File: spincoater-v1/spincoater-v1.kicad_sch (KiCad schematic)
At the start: 3 parts, among them J1 Conn_01x08_Pin, J2 SD_Card_Receptacle, U1 RASPBERRY_PI_PICO

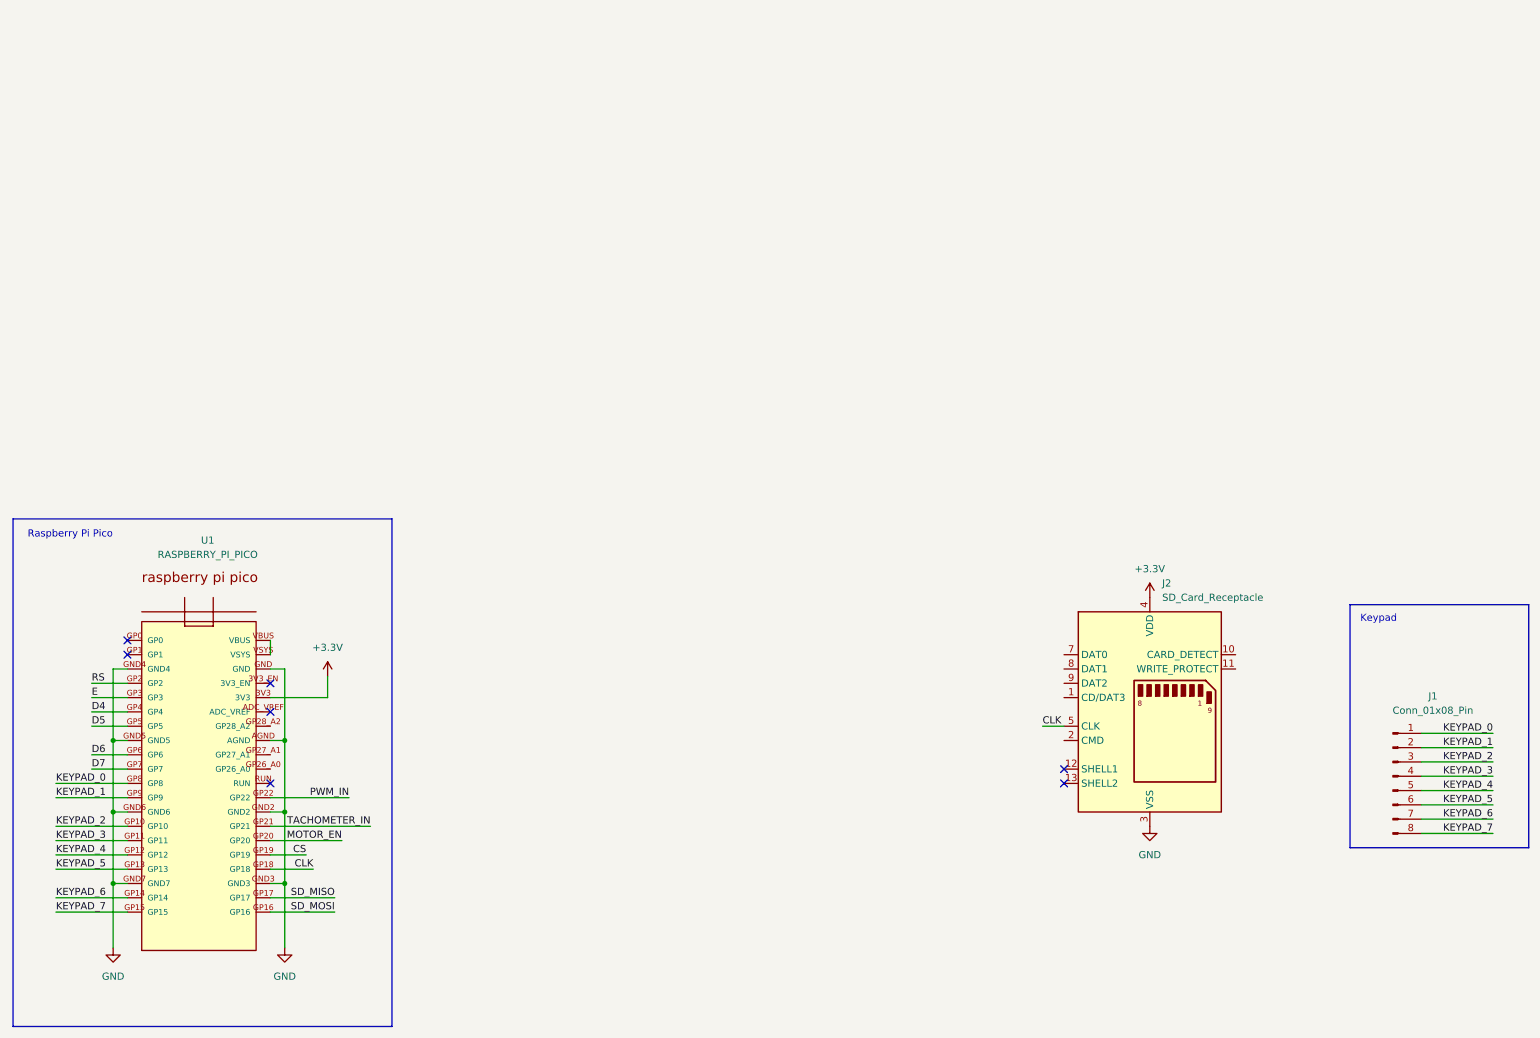
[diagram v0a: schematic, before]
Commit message: V1 schematic design of the spincoater completed.
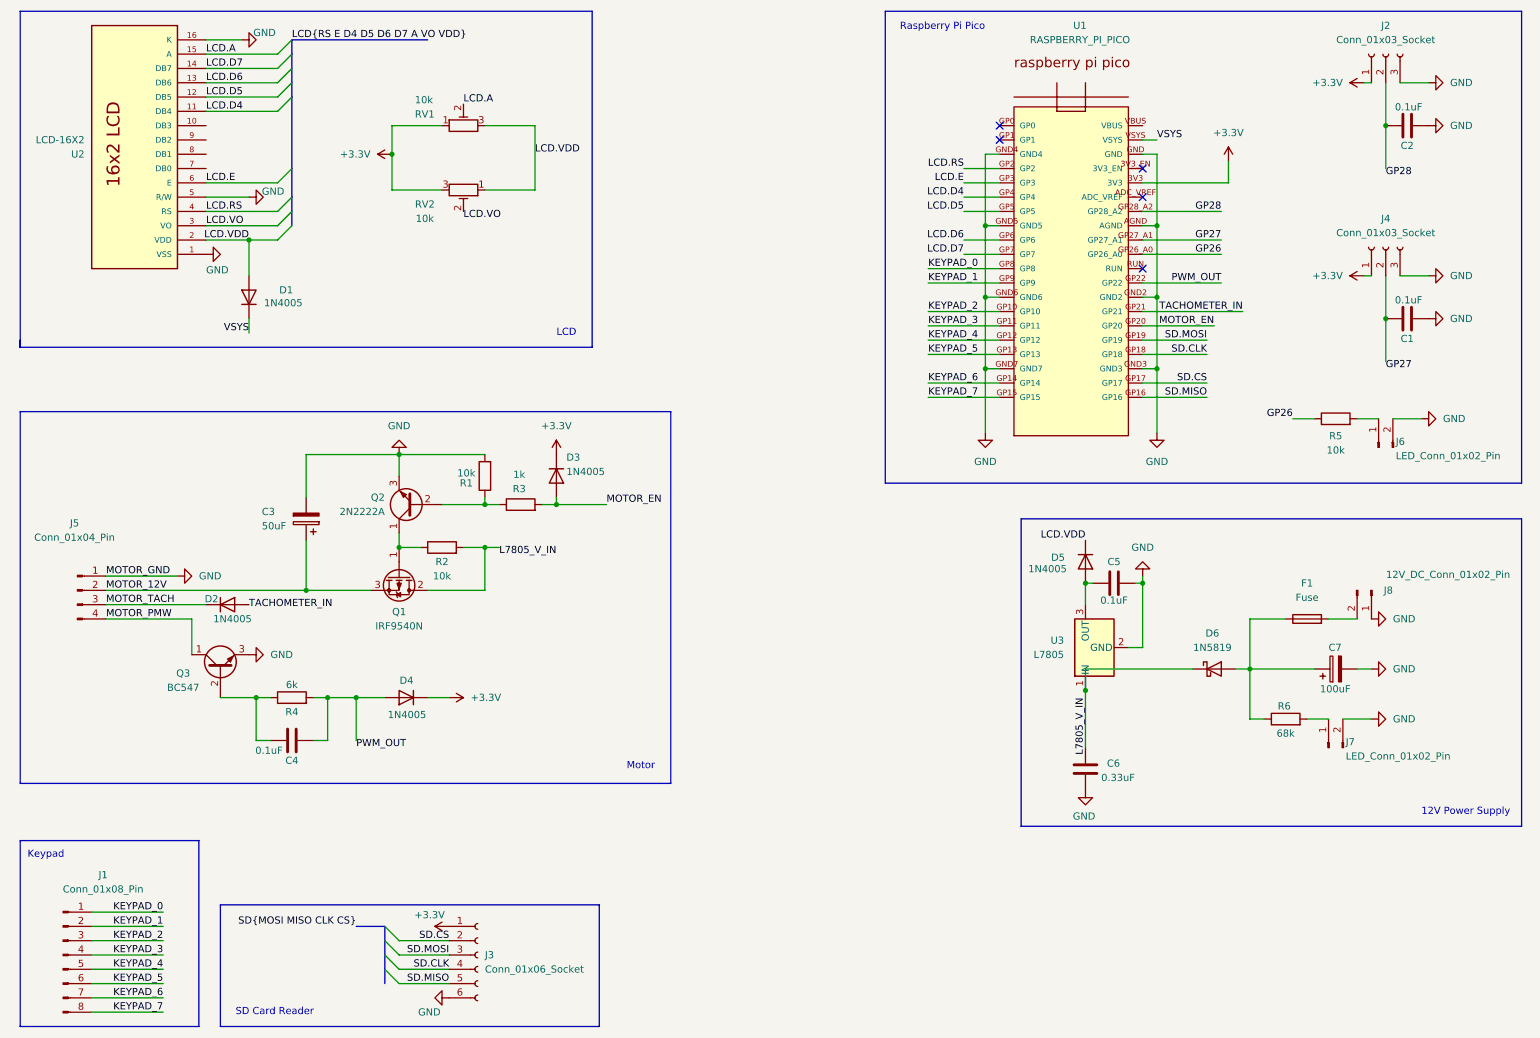
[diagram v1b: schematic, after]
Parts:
- removed J2: SD_Card_Receptacle, Connector_Card:SD_Card_Device_16mm_SlotDepth, symbol Connector:SD_Card_Receptacle
- added C1, C2, C4, C5: 0.1uF, symbol Device:C
- added C3: 50uF, symbol Device:C_Polarized
- added C6: 0.33uF, symbol Device:C
- added C7: 100uF, symbol Device:C_Polarized
- added D1, D2, D3, D4, D5: 1N4005, Diode_THT:D_DO-41_SOD81_P10.16mm_Horizontal, symbol Diode:1N4005
- added D6: 1N5819, Diode_THT:D_DO-41_SOD81_P10.16mm_Horizontal, symbol Diode:1N5819
- added F1: Fuse, symbol Device:Fuse
- added J2, J4: Conn_01x03_Socket, symbol Connector:Conn_01x03_Socket
- added J3: Conn_01x06_Socket, symbol Connector:Conn_01x06_Socket
- added J5: Conn_01x04_Pin, symbol Connector:Conn_01x04_Pin
- added J6, J7: LED_Conn_01x02_Pin, symbol Connector:Conn_01x02_Pin
- added J8: 12V_DC_Conn_01x02_Pin, symbol Connector:Conn_01x02_Pin
- added Q1: IRF9540N, Package_TO_SOT_THT:TO-220-3_Vertical, symbol Transistor_FET:IRF9540N
- added Q2: 2N2222A, Package_TO_SOT_THT:TO-92_Inline, symbol Transistor_BJT:BC547
- added Q3: BC547, Package_TO_SOT_THT:TO-92_Inline, symbol Transistor_BJT:BC547
- added R1, R2, R5: 10k, symbol Device:R
- added R3: 1k, symbol Device:R
- added R4: 6k, symbol Device:R
- added R6: 68k, symbol Device:R
- added RV1, RV2: 10k, symbol Device:R_Potentiometer_Trim
- added U2: LCD-16X2, LCD-16X2:MODULE_LCD-16X2, symbol LCD-16X2:LCD-16X2
- added U3: L7805, symbol Regulator_Linear:L7805
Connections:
- net +3.3V: now also D3.1 (K), D4.1 (K), J2.1 (Pin_1), J3.1 (Pin_1), J4.1 (Pin_1), RV1.1, RV2.3
- net GND: now also C1.2, C2.2, C3.2, C5.2, C6.1, C7.2, J2.3 (Pin_3), J3.6 (Pin_6), J4.3 (Pin_3), J5.1 (Pin_1), J6.2 (Pin_2), J7.2 (Pin_2), J8.1 (Pin_1), Q2.3 (E), Q3.3 (E), R1.2, U2.1 (VSS), U2.16 (K), U2.5 (R/W), U3.2 (GND)
- net MOTOR_EN: now also D3.2 (A), R3.2
- net TACHOMETER_IN: now also D2.2 (A)
- net GP26: now reaches U1.GP26_A0
- net GP26: now also R5.1
- net GP27: now reaches U1.GP27_A1
- net GP27: now also C1.1, J4.2 (Pin_2)
- net GP28: now reaches U1.GP28_A2
- net GP28: now also C2.1, J2.2 (Pin_2)
- net at U1.VBUS: no longer U1.VSYS
- net CLK renamed SD.CLK
- net SD.CLK: now also J3.4 (Pin_4)
- net CS renamed SD.MOSI
- net SD.MOSI: now also J3.3 (Pin_3)
- net D4 renamed LCD.D4
- net LCD.D4: now also U2.11 (DB4)
- net D5 renamed LCD.D5
- net LCD.D5: now also U2.12 (DB5)
- net D6 renamed LCD.D6
- net LCD.D6: now also U2.13 (DB6)
- net D7 renamed LCD.D7
- net LCD.D7: now also U2.14 (DB7)
- net E renamed LCD.E
- net LCD.E: now also U2.6 (E)
- net PWM_IN renamed PWM_OUT
- net PWM_OUT: now also C4.2, D4.2 (A), R4.2
- net RS renamed LCD.RS
- net LCD.RS: now also U2.4 (RS)
- net SD_MISO renamed SD.CS
- net SD.CS: now also J3.2 (Pin_2)
- net SD_MOSI renamed SD.MISO
- net SD.MISO: now also J3.5 (Pin_5)
- new net: C7.1, D6.2 (A), F1.1, R6.1
- new net: F1.2, J8.2 (Pin_2)
- new net: Q1.1 (G), Q2.1 (C), R2.1
- new net: J7.1 (Pin_1), R6.2
- new net: J6.1 (Pin_1), R5.2
- new net: C5.1, D5.2 (A), U3.3 (OUT)
- new net: C4.1, Q3.2 (B), R4.1
- new net: Q2.2 (B), R1.1, R3.1
- new net L7805_V_IN: C6.2, D6.1 (K), Q1.2 (D), R2.2, U3.1 (IN)
- new net LCD.A: RV1.2, U2.15 (A)
- new net LCD.VDD: D1.2 (A), D5.1 (K), RV1.3, RV2.1, U2.2 (VDD)
- new net LCD.VO: RV2.2, U2.3 (VO)
- new net MOTOR_12V: C3.1, J5.2 (Pin_2), Q1.3 (S)
- new net MOTOR_PMW: J5.4 (Pin_4), Q3.1 (C)
- new net MOTOR_TACH: D2.1 (K), J5.3 (Pin_3)
- new net VSYS: D1.1 (K), U1.VSYS
- no-connect marks 7 -> 5
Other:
- note added: "12V Power Supply"
- note added: "LCD"
- note added: "Motor"
- note added: "SD Card Reader"
- company: (none) -> Waterloo Hacker Fab
- title: (none) -> spincoater
- moved on the sheet: J1, U1
